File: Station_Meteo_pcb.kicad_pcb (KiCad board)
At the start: 2 copper layers, 132 parts, among them J1 ZX-FPC-FWSX0.5PH224, J10 DZ254S-11-02-48, J11 DZ254S-11-02-48, J2 GT-USB-7002A, J3 BH127VS-14P-H49, J4 DZ254S-11-02-48, J5 DZ254S-11-02-48, J6 DZ254S-11-02-48, J8 DZ254S-11-02-48, J9 DZ254S-11-02-48, Q1 AO3400A, Q2 AO3400A, Q3 AO3401A, Q5 FS8205A, Q6 AO3401A, Q7 AO3401A, Q8 AO3401A, Q9 AO3400A, U1 BME280, U2 STM32L476RGTx, U3 TP4056-42-ESOP8, U4 TPS63802DLAR, U5 DW01A, Y2 Crystal

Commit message: placement
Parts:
- moved R6 134.3 mm to (243.5, 50.0)
- moved C18 133.5 mm to (243.5, 47.3)
- moved R19 132.3 mm to (212.2, 123.4)
- moved C17 131.3 mm to (240.0, 47.0)
- moved R17 130.9 mm to (244.0, 53.0)
- moved R16 127.3 mm to (240.0, 50.0)
- moved C32 127.0 mm to (212.0, 95.0)
- moved FB1 127.0 mm to (212.0, 97.5)
- moved R18 127.0 mm to (212.0, 102.5)
- moved R7 127.0 mm to (212.0, 100.0)
- moved J8 125.9 mm to (252.0, 59.0)
- moved U5 125.9 mm to (235.0, 50.0)
- moved Q8 118.7 mm to (250.0, 53.0)
- moved Q5 114.5 mm to (240.0, 62.0)
- moved D6 114.4 mm to (245.0, 56.0)
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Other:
- board outline added: 107 x 64 mm

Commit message: t
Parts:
- moved R25 5.96 mm to (191.0, 107.1)
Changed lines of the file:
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@@
 	(footprint "Resistor_SMD:R_0603_1608Metric"
 		(layer "F.Cu")
-		(at 190.175 113)
+		(at 191 107.1)
 		(descr "Resistor SMD 0603 (1608 Metric), square (rectangular) end terminal, IPC-7351 nominal, (Body size source: IPC-SM-782 page 72, https://www.pcb-3d.com/wordpress/wp-content/uploads/ipc-sm-782a_amendment_1_and_2.pdf), generated with kicad-footprint-generator")
 		(tags "resistor")

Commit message: Placement
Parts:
- moved C18 60.1 mm to (197.5, 86.0), turned to 180 degrees
- moved R16 59.9 mm to (186.5, 77.0), turned to 180 degrees
- moved R17 58.5 mm to (189.0, 73.0), turned to 180 degrees
- moved Q5 57.3 mm to (183.5, 71.5)
- moved J8 54.4 mm to (198.3, 50.3), turned to 90 degrees
- moved Q8 54.0 mm to (204.5, 82.0)
- moved R6 53.6 mm to (196.3, 75.5)
- moved C17 50.9 mm to (196.0, 72.5), turned to 90 degrees
- moved U5 48.0 mm to (193.1, 73.5)
- moved D6 47.4 mm to (201.0, 73.5), turned to 180 degrees
- moved D7 43.2 mm to (170.5, 82.5)
- moved U3 41.9 mm to (195.3, 82.3)
- moved Q7 38.8 mm to (167.5, 85.5)
- moved C31 38.2 mm to (198.5, 91.5), turned to 180 degrees
- moved F2 37.5 mm to (175.5, 86.0)
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
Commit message: push routage
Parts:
- moved J10 10.7 mm to (192.4, 95.8), turned to -90 degrees
- moved F1 10.2 mm to (191.3, 104.5), turned to 90 degrees
- moved C33 7.18 mm to (195.6, 105.1), turned to 180 degrees
- moved C34 6.99 mm to (196.1, 107.8), turned to -90 degrees
- moved R20 6.28 mm to (201.2, 89.3)
- moved R19 4.08 mm to (199.7, 92.9)
- moved D3 3.96 mm to (196.6, 101.2)
- moved FB1 3.78 mm to (195.2, 103.5), turned to 0 degrees
- moved C32 3.69 mm to (194.4, 101.1)
- moved C31 3.63 mm to (199.0, 95.1)
- moved J2 3.60 mm to (203.0, 102.6)
- moved R18 1.75 mm to (198.2, 106.1), turned to -90 degrees
- moved R7 0.86 mm to (198.2, 103.0), turned to -90 degrees
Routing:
- net Net-(D3-K): track 0.00 -> 12.9 mm
- net Net-(C33-Pad1): track 0.00 -> 8.69 mm
- net Net-(J10-Pin_2): track 0.00 -> 4.12 mm
- net VBUS: track 0.00 -> 4.05 mm
- net Net-(J2-CC1): track 0.00 -> 3.48 mm
- net Net-(J2-CC2): track 0.00 -> 1.83 mm
- net GND1: track 0.00 -> 0.04 mm, vias 0 -> 6
- net GND: vias 0 -> 3
- added copper zone on B.Cu, net GND
- added copper zone on F.Cu, net GND
- added copper zone on B.Cu, net GND1
- added copper zone on F.Cu, net GND1

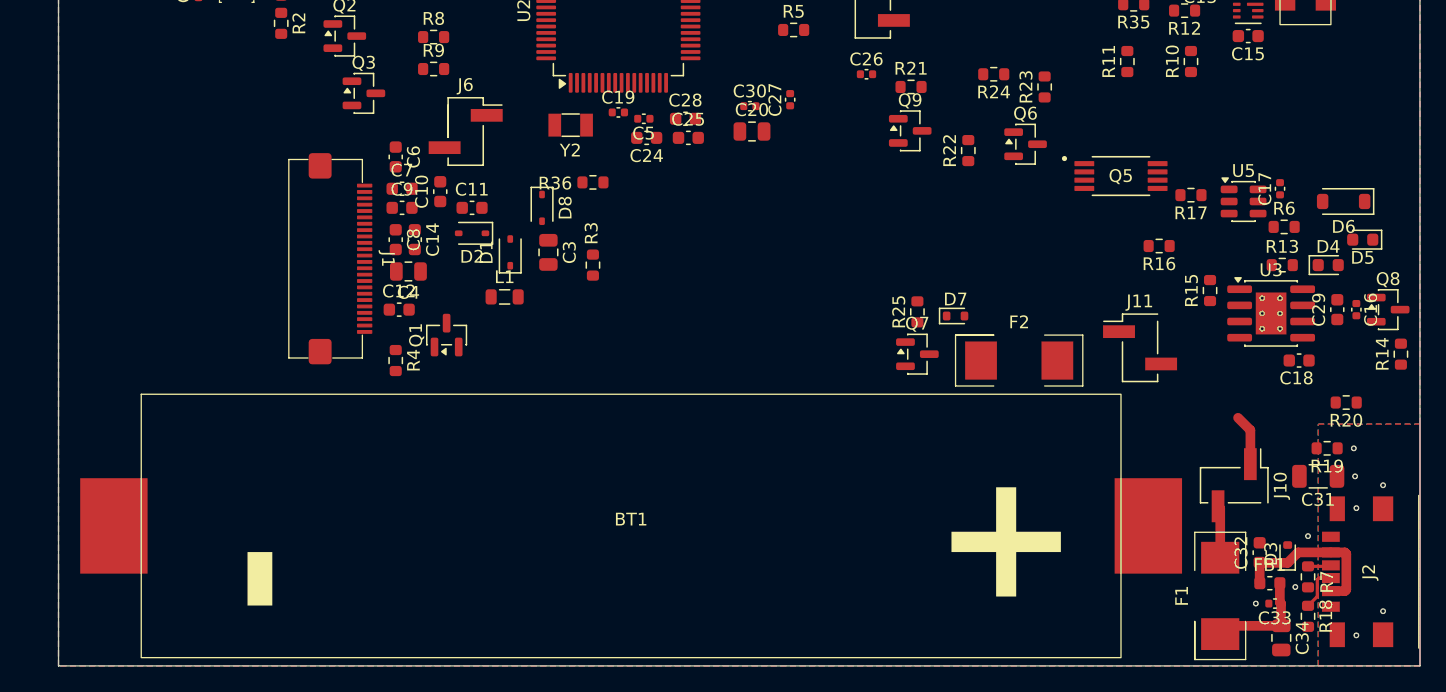
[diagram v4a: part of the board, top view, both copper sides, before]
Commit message: Suite routage (vers pile)
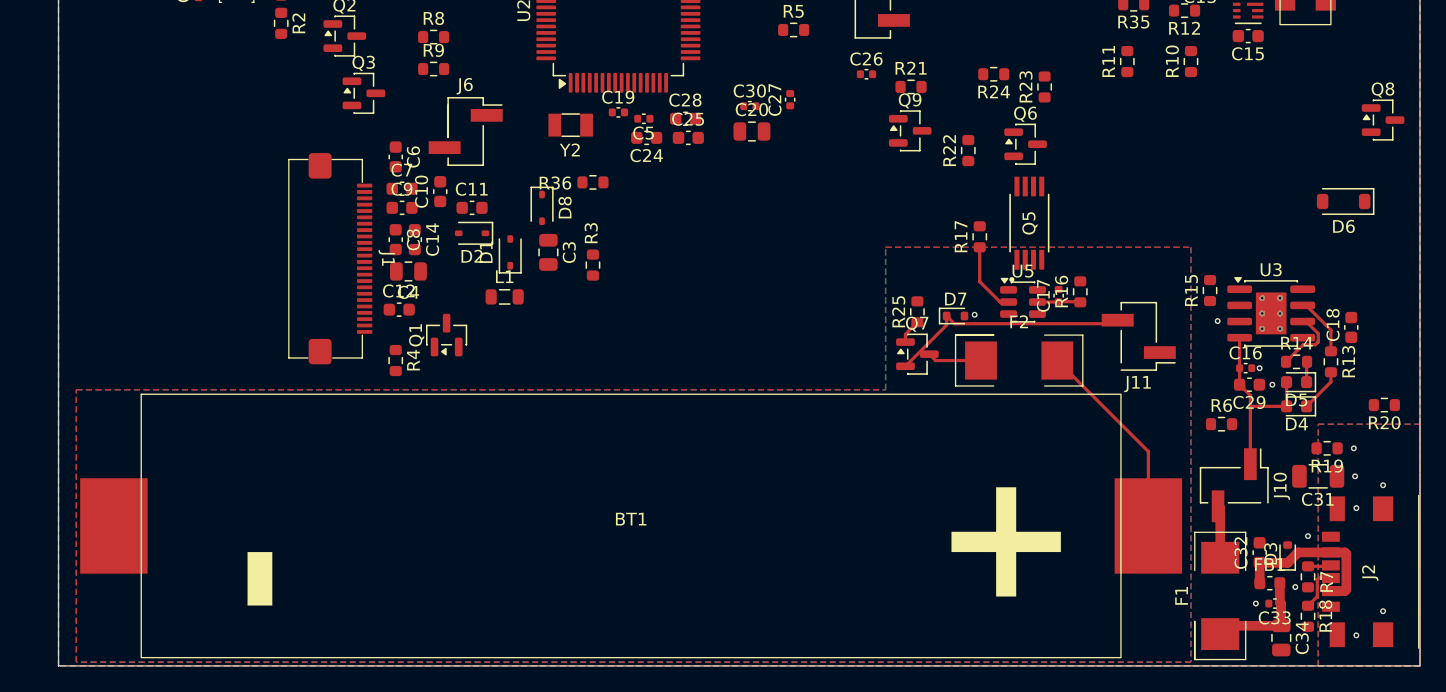
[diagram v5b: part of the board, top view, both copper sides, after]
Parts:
- moved C17 19.3 mm to (178.6, 80.9)
- moved U5 19.1 mm to (175.8, 81.4)
- moved R17 16.9 mm to (172.4, 76.3), turned to 90 degrees
- moved R6 16.3 mm to (191.4, 91.0)
- moved Q8 14.9 mm to (204.1, 67.1)
- moved D5 12.3 mm to (197.3, 87.7)
- moved D4 11.4 mm to (197.3, 89.6), turned to 180 degrees
- moved C16 9.84 mm to (193.3, 86.6), turned to 0 degrees
- moved C29 9.08 mm to (193.6, 87.9), turned to 180 degrees
- moved R13 8.51 mm to (200.0, 86.1), turned to -90 degrees
- moved R14 8.22 mm to (197.3, 86.1), turned to 0 degrees
- moved Q5 8.10 mm to (176.3, 75.2), turned to 90 degrees
- moved R16 7.17 mm to (180.3, 80.6), turned to 90 degrees
- moved C18 4.85 mm to (201.6, 83.4), turned to 90 degrees
- moved R20 3.01 mm to (204.2, 89.5)
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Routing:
- net Net-(BT1-+): track 0.00 -> 39.3 mm
- net VBUS: track 4.05 -> 15.1 mm
- net Net-(U5-CS): track 0.00 -> 5.63 mm
- net Net-(U3-~{STDBY}): track 0.00 -> 5.45 mm
- net Net-(U3-~{CHRG}): track 0.00 -> 4.70 mm
- net Net-(D4-K): track 0.00 -> 3.47 mm
- net Net-(U5-VCC): track 0.00 -> 3.39 mm
- net Net-(Q7-G): track 0.00 -> 1.94 mm
- net Net-(D5-K): track 0.00 -> 1.62 mm
- net GND: vias 3 -> 6
- net (no net): vias 0 -> 1
- added copper zone on B.Cu, net GNDA
- added copper zone on F.Cu, net GNDA

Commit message: V1 Placement + Routage
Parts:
- J2: value GT-USB-7002A -> UC18-0B06F68011
- moved Q2 38.2 mm to (154.1, 81.9), turned to -90 degrees
- moved R8 33.8 mm to (153.0, 84.9)
- moved Q3 31.9 mm to (150.0, 83.4)
- moved J5 30.9 mm to (145.9, 49.6), turned to -90 degrees
- moved R9 30.9 mm to (155.9, 79.0)
- moved R1 28.0 mm to (144.7, 63.2), turned to 180 degrees
- moved C2 27.8 mm to (138.4, 52.5), turned to 180 degrees
- moved R2 27.7 mm to (144.7, 64.8), turned to 0 degrees
- moved C1 25.4 mm to (136.3, 52.5), turned to 0 degrees
- moved U1 24.7 mm to (137.9, 50.3), turned to 0 degrees
- moved J8 23.2 mm to (202.8, 73.1), turned to 0 degrees
- moved J4 21.9 mm to (182.3, 72.8)
- moved J6 19.5 mm to (144.6, 82.8), turned to -90 degrees
- moved L2 15.6 mm to (196.5, 73.0), turned to -90 degrees
- moved C28 14.8 mm to (151.6, 52.4), turned to 180 degrees
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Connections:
- D7 pad 1: Net-(BT1-+) -> Net-(D7-K)
- F2 pad 2: Net-(BT1-+) -> Net-(Q7-D)
- J11 pad 2: Net-(BT1-+) -> Net-(D7-K)
- Q7 pad 2: Net-(BT1-+) -> Net-(D7-K)
- Q7 pad 3: Net-(BT1-+) -> Net-(Q7-D)
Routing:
- net +3V3: track 0.00 -> 182.1 mm
- net EPD_PWR: track 0.00 -> 66.3 mm, vias 0 -> 2
- net EPD_DIN: track 0.00 -> 64.4 mm, vias 0 -> 2
- net EPD_BUSY: track 0.00 -> 60.5 mm, vias 0 -> 2
- net EPD_RST: track 0.00 -> 49.9 mm, vias 0 -> 2
- net EPD_DC: track 0.00 -> 46.3 mm, vias 0 -> 2
- net EPD_CS: track 0.00 -> 44.2 mm, vias 0 -> 2
- net EPD_SCK: track 0.00 -> 44.2 mm, vias 0 -> 2
- net +BATT: track 0.00 -> 41.8 mm, vias 0 -> 2
- net VBUS: track 15.1 -> 50.5 mm
- net Net-(J9-Pin_1): track 0.00 -> 33.9 mm, vias 0 -> 2
- net nRST: track 0.00 -> 32.2 mm
- net SDA: track 0.00 -> 24.1 mm
- net MEASURE_BATTERY: track 0.00 -> 23.6 mm
- net Net-(BT1-+): track 39.3 -> 16.0 mm
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
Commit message: t
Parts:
- removed TP10, TP11, TP12, TP17, TP6, TP7, TP8, TP9: TestPoint, TestPoint:TestPoint_Pad_D1.5mm
- moved TP24 124.5 mm to (-15.1, -19.4)
- moved TP25 124.5 mm to (-15.1, -15.8)
- moved TP26 124.5 mm to (-15.1, -12.2)
- moved TP32 123.3 mm to (-15.1, -6.70)
- moved TP33 123.3 mm to (-15.1, -3.15)
- moved TP27 123.0 mm to (-20.6, -19.4)
- moved TP31 123.0 mm to (-20.6, -5.15)
- moved TP28 123.0 mm to (-20.6, -15.8)
- moved TP29 123.0 mm to (-20.6, -12.2)
- moved TP30 123.0 mm to (-20.6, -8.70)
- moved TP18 122.5 mm to (-29.7, -5.15)
- moved TP20 122.5 mm to (-26.1, -19.4)
- moved TP21 122.5 mm to (-26.1, -15.8)
- moved TP22 122.5 mm to (-26.1, -12.2)
- moved TP23 122.5 mm to (-26.1, -8.70)
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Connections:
- C4 pad 2: EPD_PWR -> ALIM_SCREEN
- C6 pad 1: EPD_PWR -> ALIM_SCREEN
- J1 pad 15: EPD_PWR -> ALIM_SCREEN
- J1 pad 16: EPD_PWR -> ALIM_SCREEN
- J6 pad 2: EPD_PWR -> ALIM_SCREEN
- L1 pad 1: EPD_PWR -> ALIM_SCREEN
- Q2 pad 1: CMD_ALIM_SCREEN -> EPD_PWR
- R9 pad 1: CMD_ALIM_SCREEN -> EPD_PWR
- TP27 pad 1: EPD_PWR -> ALIM_SCREEN
- U2 pad 8: CMD_ALIM_SCREEN -> unconnected-(U2-PC0-Pad8)
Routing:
- net +3V3: track 182.1 -> 0.00 mm
- net EPD_PWR: track 66.3 -> 0.00 mm, vias 2 -> 0
- net EPD_DIN: track 64.4 -> 13.7 mm, vias 2 -> 0
- net EPD_BUSY: track 60.5 -> 17.1 mm, vias 2 -> 0
- net EPD_RST: track 49.9 -> 16.4 mm, vias 2 -> 0
- net EPD_DC: track 46.3 -> 15.7 mm, vias 2 -> 0
- net EPD_SCK: track 44.2 -> 14.4 mm, vias 2 -> 0
- net EPD_CS: track 44.2 -> 15.0 mm, vias 2 -> 0
- net ALIM_SCREEN: track 0.00 -> 16.8 mm
- net CMD_ALIM_SCREEN: track 15.0 -> 0.00 mm
- net Net-(Q6-G): track 22.3 -> 13.1 mm
- net CMD_ALIM_BATTERY: track 8.85 -> 1.68 mm
- net VGL: track 13.1 -> 9.53 mm
- net GND: track 0.00 -> 2.45 mm, vias 30 -> 29
- net Net-(D1-A): track 16.1 -> 18.6 mm, vias 2 -> 0
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
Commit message: revue
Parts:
- moved TP21 301.2 mm to (269.9, 39.8)
- moved TP22 301.2 mm to (269.9, 43.3)
- moved TP23 301.2 mm to (269.9, 46.9)
- moved TP4 300.0 mm to (259.2, 39.8)
- moved TP5 300.0 mm to (259.2, 43.3)
- moved TP20 299.9 mm to (266.4, 46.9)
- moved TP18 299.4 mm to (266.4, 39.8)
- moved TP19 299.4 mm to (266.4, 43.3)
- moved TP1 298.4 mm to (255.7, 39.8)
- moved TP2 298.4 mm to (255.7, 43.3)
- moved TP3 298.4 mm to (255.7, 46.9)
- moved TP14 297.7 mm to (262.8, 39.8)
- moved TP15 297.7 mm to (262.8, 43.3)
- moved TP16 297.7 mm to (262.8, 46.9)
- moved TP13 296.4 mm to (259.2, 46.9)
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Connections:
- C20 pad 1: Net-(J9-Pin_1) -> 3v3s
- C21 pad 1: Net-(J9-Pin_1) -> 3v3s
- C22 pad 1: Net-(J9-Pin_1) -> 3v3s
- C23 pad 1: Net-(J9-Pin_1) -> 3v3s
- C24 pad 1: +3V3 -> 3v3s
- C25 pad 1: +3V3 -> 3v3s
- C28 pad 1: +3V3 -> 3v3s
- C30 pad 1: Net-(J9-Pin_1) -> 3v3s
- C5 pad 1: +3V3 -> 3v3s
- J9 pad 1: Net-(J9-Pin_1) -> 3v3s
- R1 pad 2: +3V3 -> Net-(J5-Pin_2)
- R2 pad 1: +3V3 -> Net-(J5-Pin_2)
- TP18 pad 1: +3V3 -> 3v3s
- TP19 pad 1: +3V3 -> 3v3s
- TP20 pad 1: +3V3 -> 3v3s
- U1 pad 2: +3V3 -> Net-(J5-Pin_2)
- U2 pad 1: Net-(J9-Pin_1) -> 3v3s
- U2 pad 13: +3V3 -> 3v3s
- U2 pad 19: Net-(J9-Pin_1) -> 3v3s
- U2 pad 32: Net-(J9-Pin_1) -> 3v3s
- U2 pad 48: +3V3 -> 3v3s
- U2 pad 64: Net-(J9-Pin_1) -> 3v3s
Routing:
- net +3V3: track 0.00 -> 129.9 mm
- net 3v3s: track 0.00 -> 82.2 mm
- net Net-(J9-Pin_1): track 33.9 -> 0.00 mm, vias 2 -> 0
- net EPD_DIN: track 13.7 -> 44.4 mm, vias 0 -> 2
- net EPD_SCK: track 14.4 -> 44.2 mm, vias 0 -> 2
- net EPD_CS: track 15.0 -> 44.2 mm, vias 0 -> 2
- net SCL: track 22.1 -> 50.4 mm, vias 0 -> 2
- net SDA: track 24.1 -> 51.9 mm, vias 0 -> 2
- net EPD_BUSY: track 17.1 -> 44.6 mm, vias 0 -> 2
- net EPD_DC: track 15.7 -> 42.9 mm, vias 0 -> 2
- net EPD_RST: track 16.4 -> 43.1 mm, vias 0 -> 2
- net EPD_PWR: track 0.00 -> 25.3 mm, vias 0 -> 2
- net nRST: track 32.2 -> 49.9 mm, vias 0 -> 2
- net SWDIO: track 16.0 -> 33.2 mm, vias 0 -> 2
- net SWCLK: track 22.0 -> 38.0 mm, vias 0 -> 2
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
